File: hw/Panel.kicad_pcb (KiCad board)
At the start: 2 copper layers, 50.8 x 128.5 mm, 24 parts

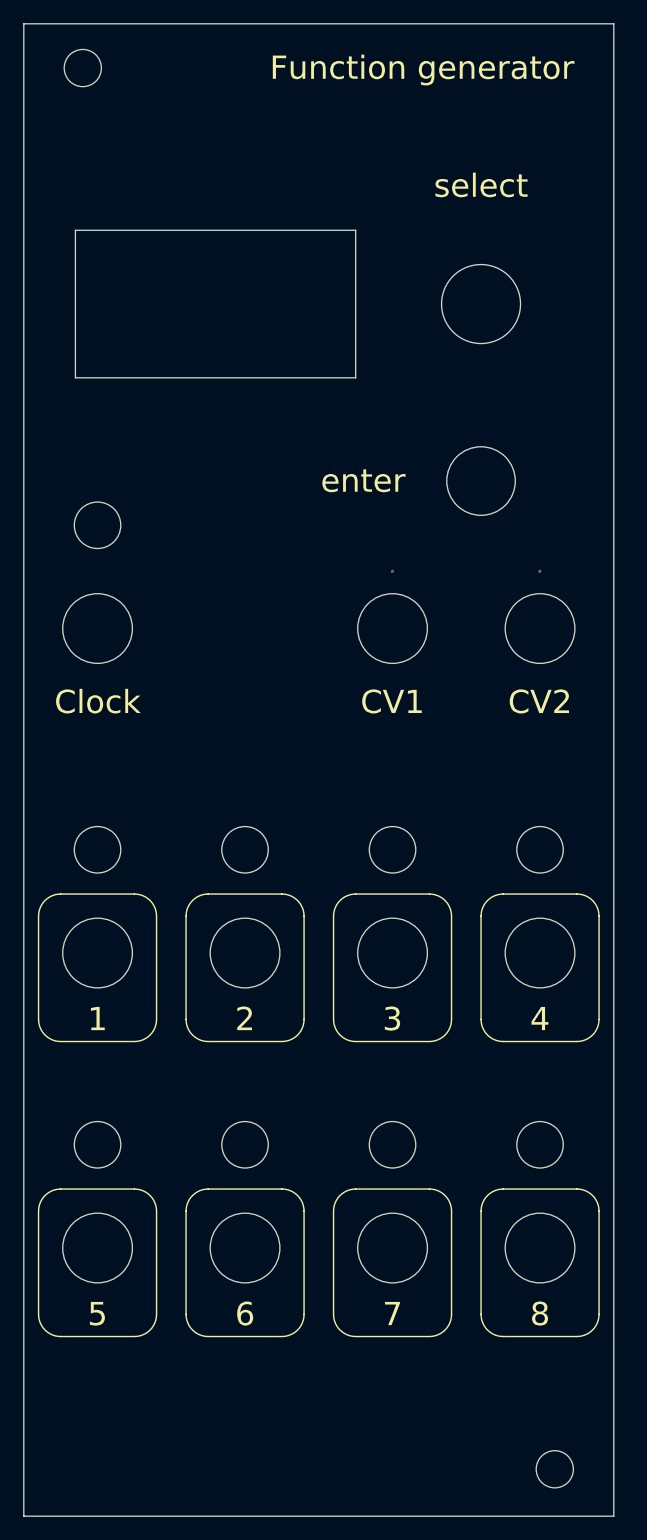
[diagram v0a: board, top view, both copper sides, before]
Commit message: Software: appended polarity selection functionality. Hardware: appended power reversal protection.           adjusted silks.
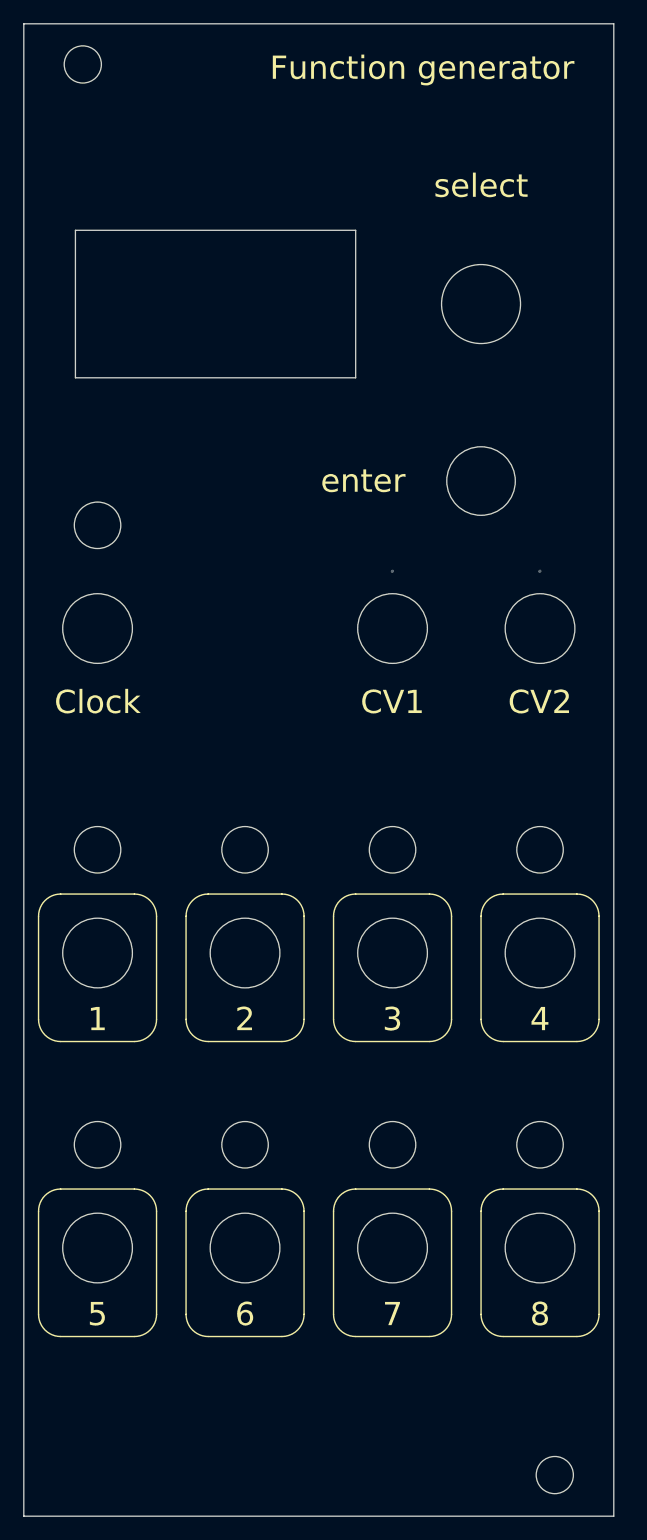
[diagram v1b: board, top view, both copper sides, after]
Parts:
- moved REF** 0.50 mm to (222.2, 156.7)
- moved REF** 0.31 mm to (181.6, 35.2)

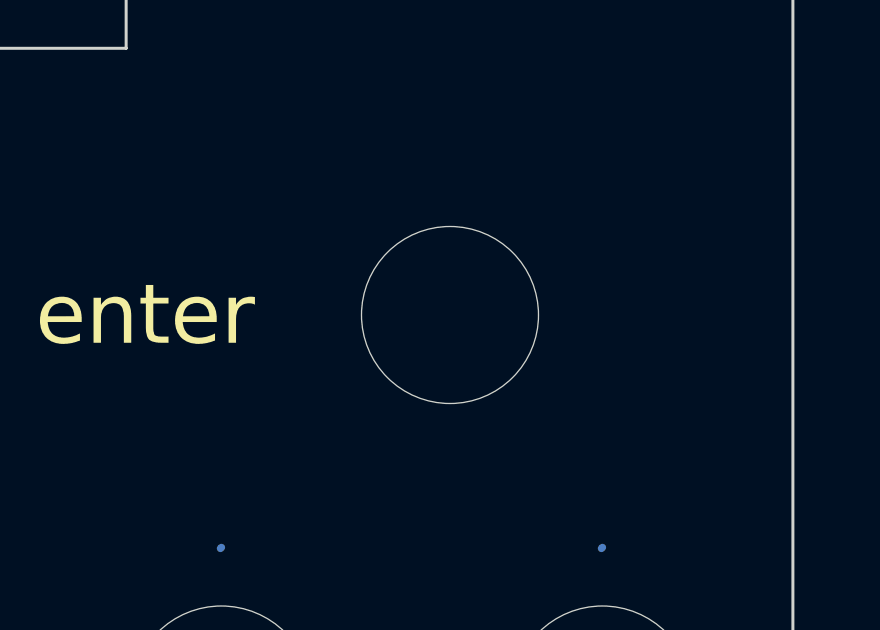
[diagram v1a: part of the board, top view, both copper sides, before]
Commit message: Software: - Added CV control, but for limited functions. - Added BPM mode.
Hardware:
- Version ordered to Elecrow.
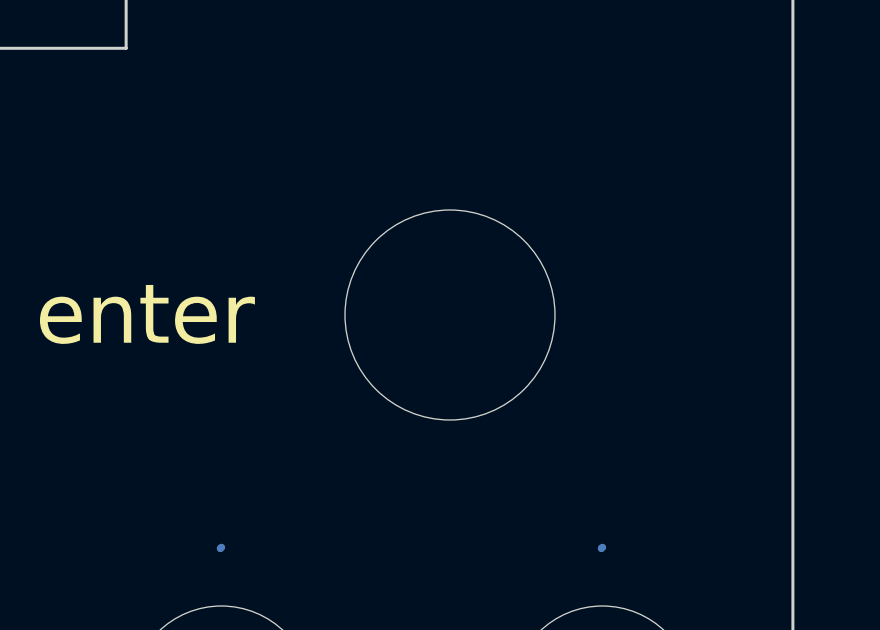
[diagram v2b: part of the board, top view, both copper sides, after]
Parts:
- removed the enter at (215.9, 71.1)
- added enter: annotation_7mm_button, Attenuverter:annotation_7mm_button, F.Cu at (215.9, 71.1)
